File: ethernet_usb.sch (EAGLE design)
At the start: 1 part, among them IC1 LAN9512

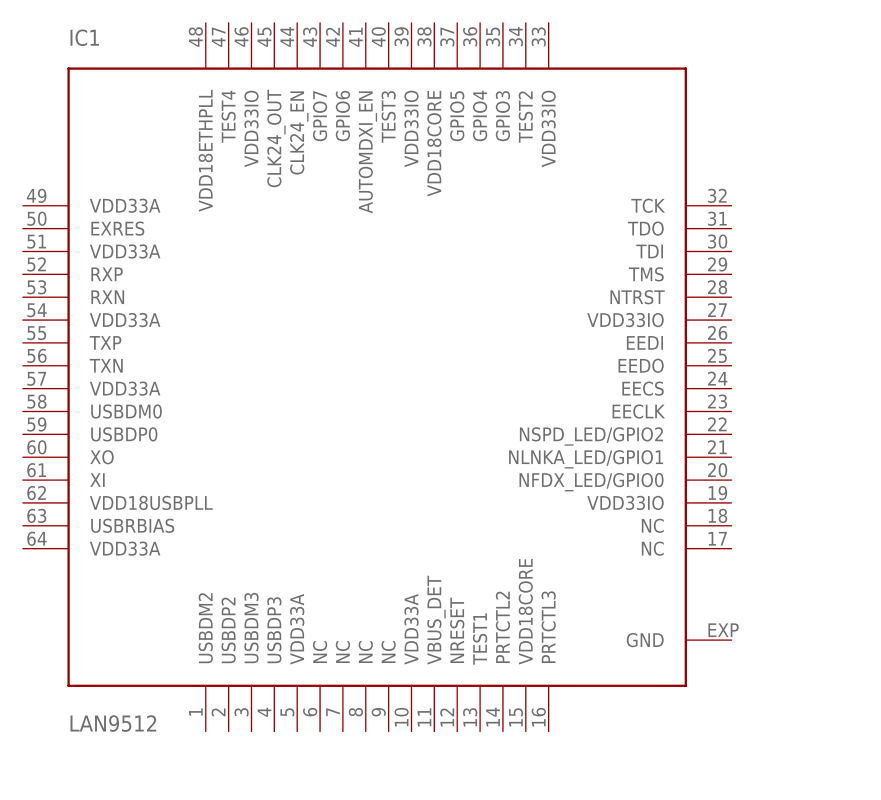
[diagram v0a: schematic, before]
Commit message: switch to LAN9514
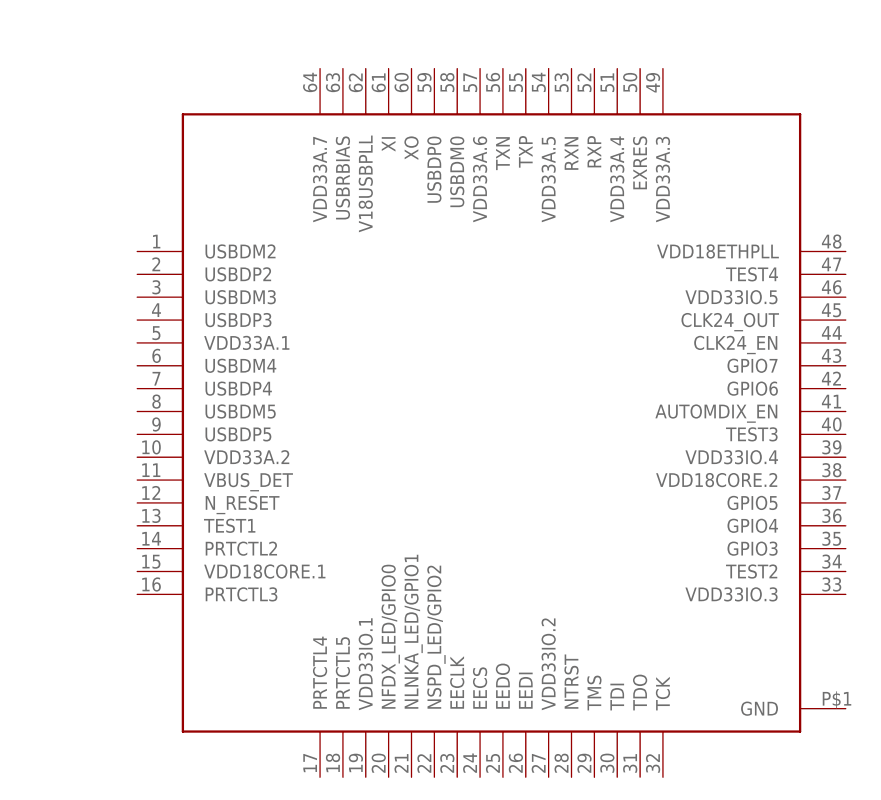
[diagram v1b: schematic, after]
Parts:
- removed IC1: LAN9512, raspberrypi_cm:LAN9512
- added U$1: LAN9514, Eagle-Library:LAN9514
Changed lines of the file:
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@@
 <layer number="54" name="bGND_GNDA" color="1" fill="9" visible="no" active="no"/>
 <layer number="56" name="wert" color="7" fill="1" visible="no" active="no"/>
+<layer number="57" name="tCAD" color="7" fill="1" visible="no" active="no"/>
 <layer number="90" name="Modules" color="5" fill="1" visible="yes" active="yes"/>
 <layer number="91" name="Nets" color="2" fill="1" visible="yes" active="yes"/>
@@
 <layer number="97" name="Info" color="7" fill="1" visible="yes" active="yes"/>
 <layer number="98" name="Guide" color="6" fill="1" visible="yes" active="yes"/>
+<layer number="99" name="SpiceOrder" color="7" fill="1" visible="yes" active="yes"/>
 <layer number="100" name="Mechanical" color="7" fill="1" visible="no" active="yes"/>
 <layer number="101" name="Gehäuse" color="7" fill="1" visible="no" active="yes"/>
 <layer number="102" name="Mittellin" color="7" fill="1" visible="no" active="yes"/>
+<layer number="103" name="tMap" color="7" fill="1" visible="yes" active="yes"/>
 <layer number="104" name="Name" color="7" fill="1" visible="no" active="yes"/>
 <layer number="105" name="Beschreib" color="9" fill="1" visible="no" active="no"/>
 <layer number="106" name="BGA-Top" color="4" fill="1" visible="no" active="no"/>
 <layer number="107" name="BD-Top" color="5" fill="1" visible="no" active="no"/>
+<layer number="108" name="tplace-old" color="10" fill="1" visible="yes" active="yes"/>
+<layer number="109" name="ref-old" color="11" fill="1" visible="yes" active="yes"/>
+<layer number="110" name="fp0" color="7" fill="1" visible="yes" active="yes"/>
+<layer number="111" name="LPC17xx" color="7" fill="1" visible="yes" active="yes"/>
+<layer number="112" name="tSilk" color="7" fill="1" visible="yes" active="yes"/>
+<layer number="113" name="IDFDebug" color="4" fill="1" visible="yes" active="yes"/>
 <layer number="116" name="Patch_BOT" color="9" fill="4" visible="yes" active="yes"/>
 <layer number="121" name="_tsilk" color="7" fill="1" visible="yes" active="yes"/>
 <layer number="122" name="_bsilk" color="7" fill="1" visible="yes" active="yes"/>
+<layer number="123" name="tTestmark" color="7" fill="1" visible="yes" active="yes"/>
+<layer number="124" name="bTestmark" color="7" fill="1" visible="yes" active="yes"/>
+<layer number="125" name="_tNames" color="7" fill="1" visible="yes" active="yes"/>
+<layer number="126" name="_bNames" color="7" fill="1" visible="yes" active="yes"/>
+<layer number="127" name="_tValues" color="7" fill="1" visible="yes" active="yes"/>
+<layer number="128" name="_bValues" color="7" fill="1" visible="yes" active="yes"/>
+<layer number="131" name="tAdjust" color="7" fill="1" visible="yes" active="yes"/>
+<layer number="132" name="bAdjust" color="7" fill="1" visible="yes" active="yes"/>
+<layer number="144" name="Drill_legend" color="7" fill="1" visible="yes" active="yes"/>
+<layer number="150" name="Notes" color="7" fill="1" visible="yes" active="yes"/>
 <layer number="151" name="HeatSink" color="7" fill="1" visible="no" active="yes"/>
+<layer number="152" name="_bDocu" color="7" fill="1" visible="yes" active="yes"/>
+<layer number="153" name="FabDoc1" color="7" fill="1" visible="yes" active="yes"/>
+<layer number="154" name="FabDoc2" color="7" fill="1" visible="yes" active="yes"/>
+<layer number="155" name="FabDoc3" color="7" fill="1" visible="yes" active="yes"/>
+<layer number="199" name="Contour" color="7" fill="1" visible="yes" active="yes"/>
 <layer number="200" name="200bmp" color="1" fill="10" visible="no" active="no"/>
 <layer number="201" name="201bmp" color="2" fill="1" visible="no" active="no"/>
 <layer number="202" name="202bmp" color="3" fill="1" visible="no" active="no"/>
+<layer number="203" name="203bmp" color="4" fill="10" visible="yes" active="yes"/>
+<layer number="204" name="204bmp" color="5" fill="10" visible="yes" active="yes"/>
+<layer number="205" name="205bmp" color="6" fill="10" visible="yes" active="yes"/>
+<layer number="206" name="206bmp" color="7" fill="10" visible="yes" active="yes"/>
+<layer number="207" name="207bmp" color="8" fill="10" visible="yes" active="yes"/>
+<layer number="208" name="208bmp" color="9" fill="10" visible="yes" active="yes"/>
+<layer number="209" name="209bmp" color="7" fill="1" visible="yes" active="yes"/>
+<layer number="210" name="210bmp" color="7" fill="1" visible="yes" active="yes"/>
+<layer number="211" name="211bmp" color="7" fill="1" visible="yes" active="yes"/>
+<layer number="212" name="212bmp" color="7" fill="1" visible="yes" active="yes"/>
+<layer number="213" name="213bmp" color="7" fill="1" visible="yes" active="yes"/>
+<layer number="214" name="214bmp" color="7" fill="1" visible="yes" active="yes"/>
+<layer number="215" name="215bmp" color="7" fill="1" visible="yes" active="yes"/>
+<layer number="216" name="216bmp" color="7" fill="1" visible="yes" active="yes"/>
+<layer number="217" name="217bmp" color="18" fill="1" visible="no" active="no"/>
+<layer number="218" name="218bmp" color="19" fill="1" visible="no" active="no"/>
+<layer number="219" name="219bmp" color="20" fill="1" visible="no" active="no"/>
+<layer number="220" name="220bmp" color="21" fill="1" visible="no" active="no"/>
+<layer number="221" name="221bmp" color="22" fill="1" visible="no" active="no"/>
+<layer number="222" name="222bmp" color="23" fill="1" visible="no" active="no"/>
+<layer number="223" name="223bmp" color="24" fill="1" visible="no" active="no"/>
+<layer number="224" name="224bmp" color="25" fill="1" visible="no" active="no"/>
+<layer number="248" name="Housing" color="7" fill="1" visible="yes" active="yes"/>
+<layer number="249" name="Edge" color="7" fill="1" visible="yes" active="yes"/>
 <layer number="250" name="Descript" color="3" fill="1" visible="no" active="no"/>
 <layer number="251" name="SMDround" color="12" fill="11" visible="no" active="no"/>
@@
 </classes>
 <parts>
-<part name="IC1" library="raspberrypi_cm" deviceset="LAN9512" device=""/>
+<part name="U$1" library="Eagle-Library" deviceset="LAN9514" device=""/>
 </parts>
 <sheets>
@@
 </plain>
 <instances>
-<instance part="IC1" gate="G$1" x="66.04" y="43.18"/>
+<instance part="U$1" gate="G$1" x="68.58" y="27.94"/>
 </instances>
 <busses>

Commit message: snapshot
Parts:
- removed U$1: LAN9514, Eagle-Library:LAN9514
- added IC1: LAN9512, raspberrypi_cm:LAN9512
- added U1: (no value), ftdichip-6:FT2232L
- added X1: MINI-USB_SHIELD4P-85-32004-10X, con-cypressindustries:MINI-USB_SHIELD4P-85-32004-10X
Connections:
- new net N$1: IC1.USBDM2, U1.USBDM
- new net N$2: IC1.USBDP2, U1.USBDP
- new net USBDMHOST: IC1.USBDM0
- new net USBDPHOST: IC1.USBDP0
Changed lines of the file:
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@@
 <layer number="2" name="Route2" color="1" fill="3" visible="no" active="no"/>
 <layer number="3" name="Route3" color="4" fill="3" visible="no" active="no"/>
+<layer number="4" name="Route4" color="1" fill="4" visible="no" active="no"/>
+<layer number="5" name="Route5" color="4" fill="4" visible="no" active="no"/>
+<layer number="6" name="Route6" color="1" fill="8" visible="no" active="no"/>
+<layer number="7" name="Route7" color="4" fill="8" visible="no" active="no"/>
+<layer number="8" name="Route8" color="1" fill="2" visible="no" active="no"/>
+<layer number="9" name="Route9" color="4" fill="2" visible="no" active="no"/>
+<layer number="10" name="Route10" color="1" fill="7" visible="no" active="no"/>
+<layer number="11" name="Route11" color="4" fill="7" visible="no" active="no"/>
+<layer number="12" name="Route12" color="1" fill="5" visible="no" active="no"/>
+<layer number="13" name="Route13" color="4" fill="5" visible="no" active="no"/>
 <layer number="14" name="Route14" color="1" fill="6" visible="no" active="no"/>
 <layer number="15" name="Route15" color="4" fill="6" visible="no" active="no"/>
@@
 </classes>
 <parts>
-<part name="U$1" library="Eagle-Library" deviceset="LAN9514" device=""/>
+<part name="U1" library="ftdichip-6" deviceset="FT2232L" device=""/>
+<part name="IC1" library="raspberrypi_cm" deviceset="LAN9512" device=""/>
+<part name="X1" library="con-cypressindustries" deviceset="MINI-USB_SHIELD4P-" device="85-32004-10X"/>
 </parts>
 <sheets>
@@
 </plain>
 <instances>
-<instance part="U$1" gate="G$1" x="68.58" y="27.94"/>
+<instance part="U1" gate="G$1" x="-546.1" y="403.86"/>
+<instance part="IC1" gate="G$1" x="-546.1" y="294.64"/>
+<instance part="X1" gate="G$1" x="-662.94" y="289.56" rot="MR0"/>
 </instances>
 <busses>
 </busses>
 <nets>
+<net name="USBDMHOST" class="0">
+<segment>
+<wire x1="-584.2" y1="289.56" x2="-617.22" y2="289.56" width="0.1524" layer="91"/>
+<pinref part="IC1" gate="G$1" pin="USBDM0"/>
+</segment>
+</net>
+<net name="USBDPHOST" class="0">
+<segment>
+<wire x1="-584.2" y1="287.02" x2="-614.68" y2="287.02" width="0.1524" layer="91"/>
+<pinref part="IC1" gate="G$1" pin="USBDP0"/>
+</segment>
+</net>
+<net name="N$1" class="0">
+<segment>
+<pinref part="IC1" gate="G$1" pin="USBDM2"/>
+<wire x1="-563.88" y1="254" x2="-563.88" y2="248.92" width="0.1524" layer="91"/>
+<wire x1="-563.88" y1="248.92" x2="-607.06" y2="248.92" width="0.1524" layer="91"/>
+<wire x1="-607.06" y1="248.92" x2="-607.06" y2="424.18" width="0.1524" layer="91"/>
+<pinref part="U1" gate="G$1" pin="USBDM"/>
+<wire x1="-607.06" y1="424.18" x2="-571.5" y2="424.18" width="0.1524" layer="91"/>
+</segment>
+</net>
+<net name="N$2" class="0">
+<segment>
+<pinref part="IC1" gate="G$1" pin="USBDP2"/>
+<wire x1="-561.34" y1="254" x2="-561.34" y2="246.38" width="0.1524" layer="91"/>
+<wire x1="-561.34" y1="246.38" x2="-609.6" y2="246.38" width="0.1524" layer="91"/>
+<wire x1="-609.6" y1="246.38" x2="-609.6" y2="416.56" width="0.1524" layer="91"/>
+<pinref part="U1" gate="G$1" pin="USBDP"/>
+<wire x1="-571.5" y1="416.56" x2="-609.6" y2="416.56" width="0.1524" layer="91"/>
+</segment>
+</net>
 </nets>
 </sheet>

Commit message: snapshot
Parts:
- added C1: 0.1uF, SparkFun-Capacitors:0.1UF-0603-25V-(+80/-20%)
- added C2: 1.0uF, SparkFun-Capacitors:1.0UF-1206-50V-10%
- added FB1: 30Ω/1.8A, SparkFun-Coils:FERRITE_BEAD-0603
- added U$1: STM32F4V_100PIN_GENERIC, stm32f4:STM32F4V_100PIN_GENERIC
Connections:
- new net GND: C2.2
- new net N$3: FB1.1, X1G$1.1
- new net V_USB: C2.1, FB1.2
- net USBDMHOST: now also X1G$1.2
- net USBDPHOST: now also X1G$1.3
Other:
- moved on the sheet: X1
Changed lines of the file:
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@@
 <layer number="56" name="wert" color="7" fill="1" visible="no" active="no"/>
 <layer number="57" name="tCAD" color="7" fill="1" visible="no" active="no"/>
+<layer number="59" name="tCarbon" color="7" fill="1" visible="no" active="no"/>
+<layer number="60" name="bCarbon" color="7" fill="1" visible="no" active="no"/>
 <layer number="90" name="Modules" color="5" fill="1" visible="yes" active="yes"/>
 <layer number="91" name="Nets" color="2" fill="1" visible="yes" active="yes"/>
@@
 <layer number="112" name="tSilk" color="7" fill="1" visible="yes" active="yes"/>
 <layer number="113" name="IDFDebug" color="4" fill="1" visible="yes" active="yes"/>
+<layer number="114" name="Badge_Outline" color="7" fill="1" visible="no" active="yes"/>
+<layer number="115" name="ReferenceISLANDS" color="7" fill="1" visible="no" active="yes"/>
 <layer number="116" name="Patch_BOT" color="9" fill="4" visible="yes" active="yes"/>
+<layer number="118" name="Rect_Pads" color="7" fill="1" visible="no" active="yes"/>
 <layer number="121" name="_tsilk" color="7" fill="1" visible="yes" active="yes"/>
 <layer number="122" name="_bsilk" color="7" fill="1" visible="yes" active="yes"/>
@@
 <layer number="127" name="_tValues" color="7" fill="1" visible="yes" active="yes"/>
 <layer number="128" name="_bValues" color="7" fill="1" visible="yes" active="yes"/>
+<layer number="129" name="Mask" color="7" fill="1" visible="yes" active="yes"/>
 <layer number="131" name="tAdjust" color="7" fill="1" visible="yes" active="yes"/>
 <layer number="132" name="bAdjust" color="7" fill="1" visible="yes" active="yes"/>
@@
 <layer number="223" name="223bmp" color="24" fill="1" visible="no" active="no"/>
 <layer number="224" name="224bmp" color="25" fill="1" visible="no" active="no"/>
+<layer number="225" name="225bmp" color="7" fill="1" visible="yes" active="yes"/>
+<layer number="226" name="226bmp" color="7" fill="1" visible="yes" active="yes"/>
+<layer number="227" name="227bmp" color="7" fill="1" visible="yes" active="yes"/>
+<layer number="228" name="228bmp" color="7" fill="1" visible="yes" active="yes"/>
+<layer number="229" name="229bmp" color="7" fill="1" visible="yes" active="yes"/>
+<layer number="230" name="230bmp" color="7" fill="1" visible="yes" active="yes"/>
+<layer number="231" name="231bmp" color="7" fill="1" visible="yes" active="yes"/>
 <layer number="248" name="Housing" color="7" fill="1" visible="yes" active="yes"/>
 <layer number="249" name="Edge" color="7" fill="1" visible="yes" active="yes"/>
@@
 <layer number="251" name="SMDround" color="12" fill="11" visible="no" active="no"/>
 <layer number="254" name="OrgLBR" color="7" fill="1" visible="no" active="yes"/>
+<layer number="255" name="routoute" color="7" fill="1" visible="yes" active="yes"/>
 </layers>
 <schematic xreflabel="%F%N/%S.%C%R" xrefpart="/%S.%C%R">
@@
 <part name="IC1" library="raspberrypi_cm" deviceset="LAN9512" device=""/>
 <part name="X1" library="con-cypressindustries" deviceset="MINI-USB_SHIELD4P-" device="85-32004-10X"/>
+<part name="U$1" library="stm32f4" deviceset="STM32F4V_100PIN_GENERIC" device=""/>
+<part name="C1" library="SparkFun-Capacitors" deviceset="0.1UF" device="-0603-25V-(+80/-20%)" value="0.1uF"/>
+<part name="C2" library="SparkFun-Capacitors" deviceset="1.0UF" device="-1206-50V-10%" value="1.0uF"/>
+<part name="FB1" library="SparkFun-Coils" deviceset="FERRITE_BEAD" device="-0603" value="30Ω/1.8A"/>
+<part name="GND1" library="SparkFun-PowerSymbols" deviceset="GND" device=""/>
+<part name="SUPPLY2" library="SparkFun-PowerSymbols" deviceset="V_USB" device=""/>
+<part name="GND2" library="SparkFun-PowerSymbols" deviceset="GND" device=""/>
+<part name="GND3" library="SparkFun-PowerSymbols" deviceset="GND" device=""/>
 </parts>
 <sheets>
@@
 <instance part="U1" gate="G$1" x="-546.1" y="403.86"/>
 <instance part="IC1" gate="G$1" x="-546.1" y="294.64"/>
-<instance part="X1" gate="G$1" x="-662.94" y="289.56" rot="MR0"/>
+<instance part="X1" gate="G$1" x="-665.48" y="287.02" rot="MR0"/>
+<instance part="U$1" gate="G$1" x="-784.86" y="381"/>
+<instance part="C1" gate="G$1" x="-647.7" y="271.78"/>
+<instance part="C2" gate="G$1" x="-637.54" y="314.96"/>
+<instance part="FB1" gate="G$1" x="-650.24" y="322.58" rot="R90"/>
+<instance part="GND1" gate="1" x="-657.86" y="266.7" smashed="yes">
+<attribute name="VALUE" x="-657.86" y="266.446" size="1.778" layer="96" align="top-center"/>
+</instance>
+<instance part="SUPPLY2" gate="G$1" x="-637.54" y="325.12"/>
+<instance part="GND2" gate="1" x="-637.54" y="307.34"/>
+<instance part="X1" gate="S" x="-668.02" y="279.4" rot="MR0"/>
+<instance part="GND3" gate="1" x="-627.38" y="266.7"/>
 </instances>
 <busses>
@@
 <net name="USBDMHOST" class="0">
 <segment>
-<wire x1="-584.2" y1="289.56" x2="-617.22" y2="289.56" width="0.1524" layer="91"/>
 <pinref part="IC1" gate="G$1" pin="USBDM0"/>
+<pinref part="X1" gate="G$1" pin="2"/>
+<wire x1="-584.2" y1="289.56" x2="-660.4" y2="289.56" width="0.1524" layer="91"/>
 </segment>
 </net>
 <net name="USBDPHOST" class="0">
 <segment>
-<wire x1="-584.2" y1="287.02" x2="-614.68" y2="287.02" width="0.1524" layer="91"/>
 <pinref part="IC1" gate="G$1" pin="USBDP0"/>
+<pinref part="X1" gate="G$1" pin="3"/>
+<wire x1="-584.2" y1="287.02" x2="-660.4" y2="287.02" width="0.1524" layer="91"/>
 </segment>
 </net>
@@
 </segment>
 </net>
+<net name="N$3" class="0">
+<segment>
+<pinref part="FB1" gate="G$1" pin="1"/>
+<wire x1="-655.32" y1="322.58" x2="-657.86" y2="322.58" width="0.1524" layer="91"/>
+<wire x1="-657.86" y1="322.58" x2="-657.86" y2="292.1" width="0.1524" layer="91"/>
+<pinref part="X1" gate="G$1" pin="1"/>
+<wire x1="-657.86" y1="292.1" x2="-660.4" y2="292.1" width="0.1524" layer="91"/>
+</segment>
+</net>
+<net name="V_USB" class="0">
+<segment>
+<pinref part="C2" gate="G$1" pin="1"/>
+<wire x1="-637.54" y1="325.12" x2="-637.54" y2="322.58" width="0.1524" layer="91"/>
+<pinref part="FB1" gate="G$1" pin="2"/>
+<wire x1="-637.54" y1="322.58" x2="-637.54" y2="320.04" width="0.1524" layer="91"/>
+<wire x1="-645.16" y1="322.58" x2="-637.54" y2="322.58" width="0.1524" layer="91"/>
+<junction x="-637.54" y="322.58"/>
+<pinref part="SUPPLY2" gate="G$1" pin="V_USB"/>
+</segment>
+</net>
+<net name="GND" class="0">
+<segment>
+<pinref part="GND2" gate="1" pin="GND"/>
+<pinref part="C2" gate="G$1" pin="2"/>
+<wire x1="-637.54" y1="309.88" x2="-637.54" y2="312.42" width="0.1524" layer="91"/>
+</segment>
+</net>

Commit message: snapshot
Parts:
- removed IC1: LAN9512, raspberrypi_cm:LAN9512
- added C3, C4: 1.0uF, SparkFun-Capacitors:1.0UF-0805-25V-10%
- added R1: 0.75, SparkFun-Resistors:0.75OHM-0805-1/4W-1%
- added U$2: LAN9514, Eagle-Library:LAN9514
- added Y1: 32.768kHz, SparkFun-Clocks:CRYSTAL-32.768KHZPTH-2X6
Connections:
- new net ETH_RXN: U$2.RXN
- new net ETH_RXP: U$2.RXP
- new net ETH_TXN: U$2.TXN
- new net ETH_TXP: U$2.TXP
- new net N$10: C3.1, R1.1, U$2.XO, Y1.1
- new net N$4: U$2.VDD18CORE.1, U$2.VDD18CORE.2
- new net N$5: U$2.VDD18ETHPLL
- new net N$6: U$2.VDD33A.1, U$2.VDD33A.2, U$2.VDD33A.3, U$2.VDD33A.4, U$2.VDD33A.5, U$2.VDD33A.6, U$2.VDD33A.7
- new net N$7: U$2.V18USBPLL
- new net N$8: U$2.VDD33IO.1, U$2.VDD33IO.2, U$2.VDD33IO.3, U$2.VDD33IO.4, U$2.VDD33IO.5
- new net N$9: C4.1, R1.2, U$2.XI, Y1.2
- net GND: now also C3.2, C4.2
- net N$1: now also U$2.USBDM2; no longer IC1.USBDM2
- net N$2: now also U$2.USBDP2; no longer IC1.USBDP2
- net USBDMHOST: now also U$2.USBDM0; no longer IC1.USBDM0
- net USBDPHOST: now also U$2.USBDP0; no longer IC1.USBDP0
